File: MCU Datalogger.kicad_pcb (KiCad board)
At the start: 2 copper layers, 52.1 x 34.3 mm, 29 parts, among them J1 Conn_01x09_Pin, J2 Conn_01x04_Pin, J3 Conn_01x04_Pin, J4 Conn_02x03_Odd_Even, U1 24LC1025, U2 DS1337S_, U3 24LC1025, U4 ATMEGA328P-AU, Y1 32.768 KHz, Y2 16MHz

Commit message: Changes in Files.
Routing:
- net /SCK: track 0.00 -> 29.2 mm
- net /SDA: track 0.00 -> 17.6 mm
- net Net-(BT1-+): track 0.00 -> 13.3 mm
- net Net-(U2-SQW/~INT): track 0.00 -> 7.32 mm
- net Net-(U2-X2): track 0.00 -> 6.99 mm
- net Net-(U2-X1): track 0.00 -> 5.36 mm
- net Net-(U2-~{INTA}): track 0.00 -> 4.76 mm

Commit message: Completed wirings.
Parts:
- moved J1 1.27 mm to (94.6, 84.5)
- moved J3 1.27 mm to (120.0, 84.5)
- turned Y2 to 180 degrees
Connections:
- C5 pad 1: Net-(BT1-+) -> /Vcc
- D2 pad 2: Net-(BT1-+) -> /Vcc
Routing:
- net /SCK: track 29.2 -> 105.0 mm, vias 0 -> 7
- net /SDA: track 17.6 -> 69.6 mm, vias 0 -> 3
- net /TX: track 0.00 -> 36.8 mm
- net /RX: track 0.00 -> 33.8 mm
- net /D2: track 0.00 -> 32.7 mm
- net /D3: track 0.00 -> 28.0 mm
- net Net-(U4-PB6): track 0.00 -> 26.9 mm, vias 0 -> 3
- net /MOSI: track 0.00 -> 24.8 mm, vias 0 -> 2
- net /D4: track 0.00 -> 24.3 mm
- net /RESET: track 0.00 -> 24.3 mm, vias 0 -> 2
- net Net-(U4-PB7): track 0.00 -> 23.1 mm, vias 0 -> 3
- net /MISO: track 0.00 -> 20.9 mm, vias 0 -> 2
- net Net-(U4-AREF): track 0.00 -> 20.3 mm, vias 0 -> 2
- net /D8: track 0.00 -> 18.8 mm
- net /D7: track 0.00 -> 18.8 mm
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
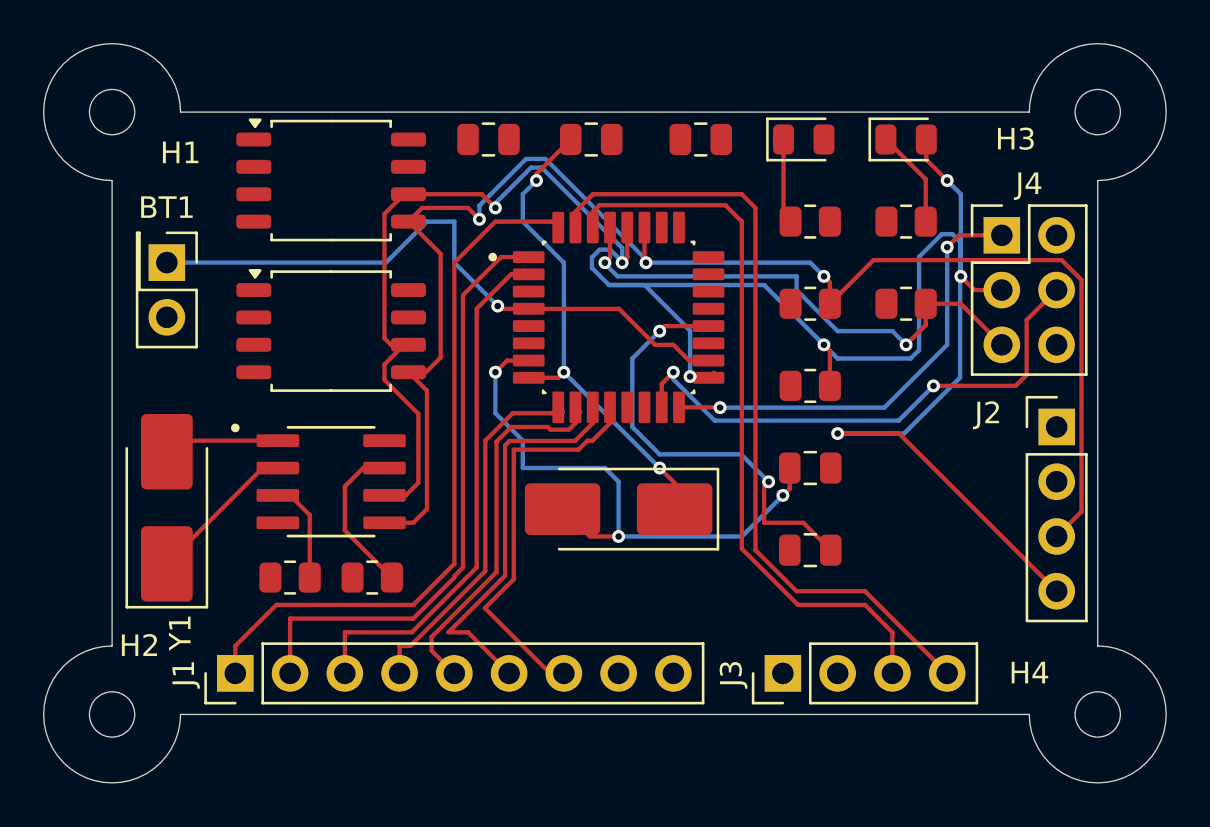
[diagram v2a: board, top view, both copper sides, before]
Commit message: Completed copper zones.
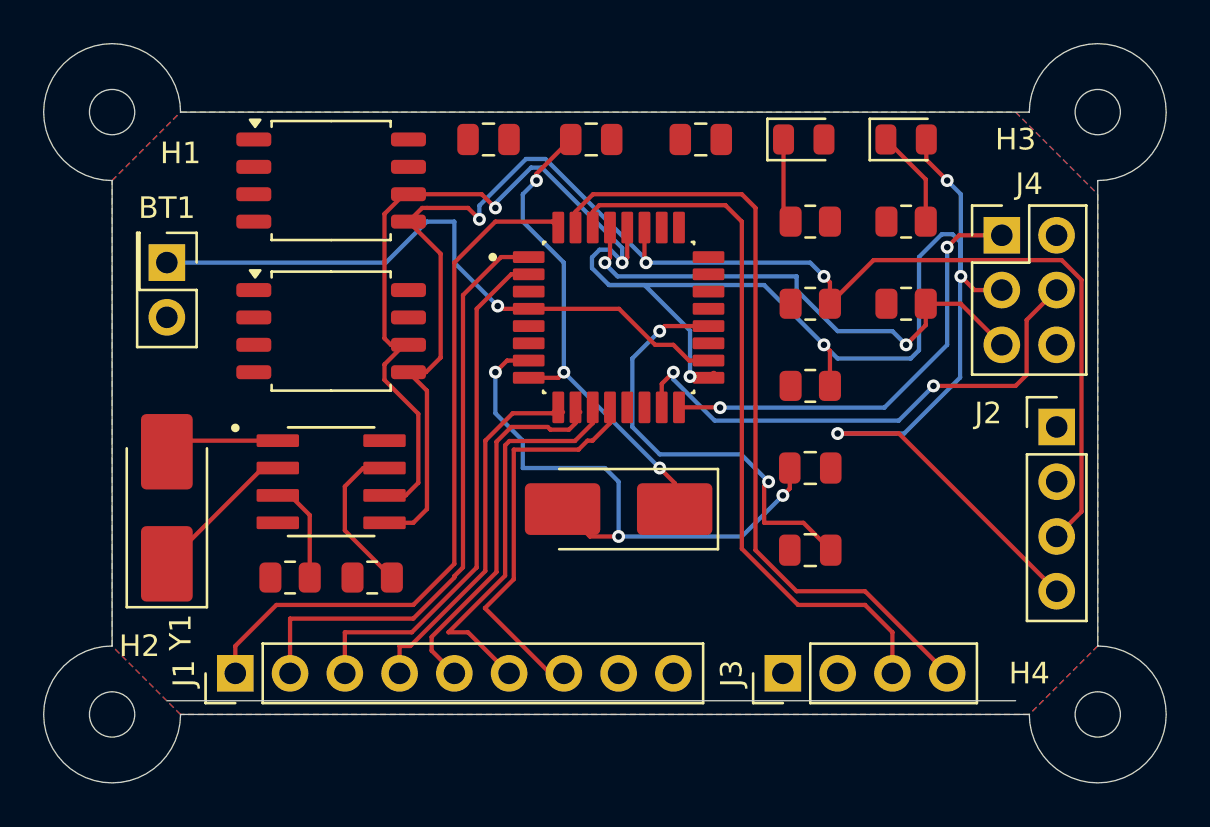
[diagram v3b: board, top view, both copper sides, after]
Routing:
- added copper zone on F.Cu, net /Vcc
- added copper zone on B.Cu, net GND
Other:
- outline, holes or cut-outs redrawn
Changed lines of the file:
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@@
+		(layer "Edge.Cuts")
+	)
+	(gr_line
+		(start 130.81 85.725)
+		(end 91.44 85.725)
+		(stroke
+			(width 0.05)
+			(type default)
+		)
 		(layer "Edge.Cuts")
 	)
@@
 		(net 26)
 	)
+	(zone
+		(net 3)
+		(net_name "/Vcc")
+		(layer "F.Cu")
+		(hatch edge 0.5)
+		(connect_pads
+			(clearance 0.5)
+		)
+		(min_thickness 0.25)
+		(filled_areas_thickness no)
+		(fill
+			(mode hatch)
+			(thermal_gap 0.5)
+			(thermal_bridge_width 0.5)
+			(hatch_thickness 1)
+			(hatch_gap 1.5)
+			(hatch_orientation 0)
+			(hatch_border_algorithm hatch_thickness)
+			(hatch_min_hole_area 0.3)
+		)
+		(polygon
+			(pts
+				(xy 88.9 61.595) (xy 92.075 58.42) (xy 130.81 58.42) (xy 134.62 62.23) (xy 134.62 83.185) (xy 131.445 86.36)
+				(xy 92.075 86.36) (xy 88.9 83.185)
+			)
+		)
+	)
+	(zone
+		(net 1)
+		(net_name "GND")
+		(layer "B.Cu")
+		(hatch edge 0.5)
+		(connect_pads
+			(clearance 0.5)
+		)
+		(min_thickness 0.25)
+		(filled_areas_thickness no)
+		(fill
+			(mode hatch)
+			(thermal_gap 0.5)
+			(thermal_bridge_width 0.5)
+			(hatch_thickness 1)
+			(hatch_gap 1.5)
+			(hatch_orientation 0)
+			(hatch_border_algorithm hatch_thickness)
+			(hatch_min_hole_area 0.3)
+		)
+		(polygon
+			(pts
+				(xy 88.9 61.595) (xy 92.075 58.42) (xy 130.81 58.42) (xy 134.62 62.23) (xy 134.62 83.185) (xy 131.445 86.36)
+				(xy 92.075 86.36) (xy 88.9 83.185)
+			)
+		)
+	)
 	(embedded_fonts no)

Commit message: Refined routing completed.
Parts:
- turned R5 to 180 degrees
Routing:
- net /Vcc: track 0.19 -> 138.8 mm, vias 0 -> 6
- net GND: track 0.00 -> 91.0 mm, vias 0 -> 11
- net /SCK: track 105.0 -> 116.9 mm, vias 7 -> 9
- net Net-(D2-K): track 3.95 -> 5.19 mm, vias 0 -> 2
- net Net-(D1-K): track 4.58 -> 3.82 mm
- net Net-(U2-X2): track 6.99 -> 7.36 mm, vias 0 -> 2
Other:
- outline, holes or cut-outs redrawn

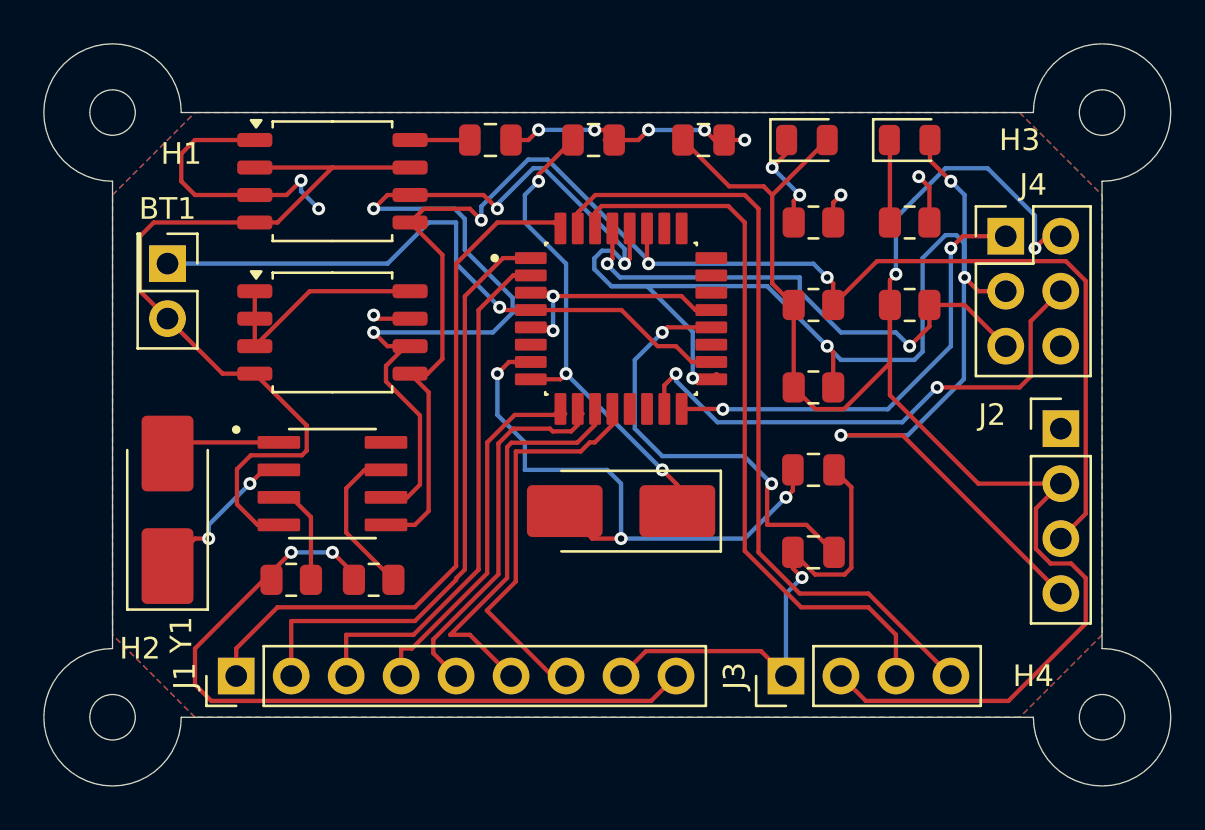
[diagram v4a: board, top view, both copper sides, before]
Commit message: Completed text references and value.
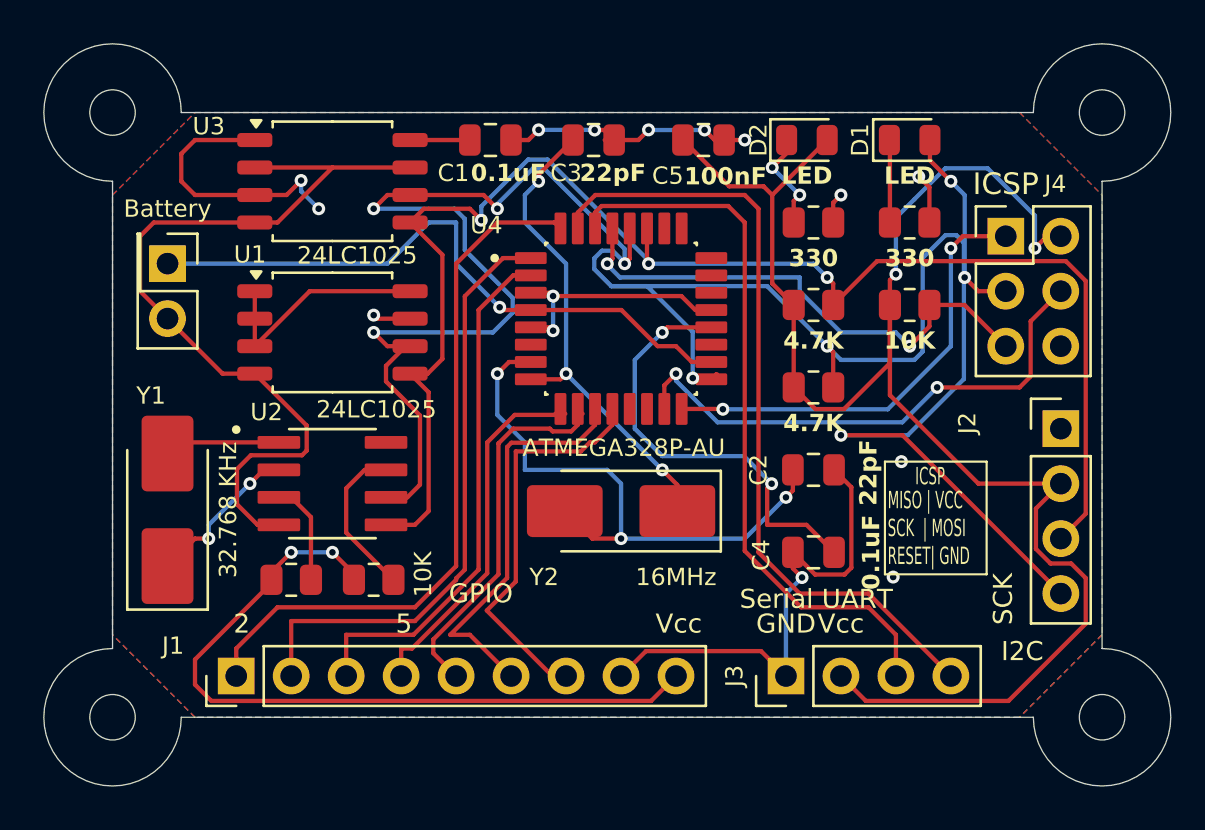
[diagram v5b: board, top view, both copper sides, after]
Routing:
- net (no net): vias 0 -> 2
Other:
- board text added: "ICSP"
- board text added: "MISO | VCC SCK | MOSI RESET| GND"

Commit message: Completed 2 layer.
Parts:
- added REF**: Symbol_GNU-Logo_SilkscreenTop, Symbol:Symbol_GNU-Logo_SilkscreenTop, B.Cu at (102.5, 74.0)
- added REF**: KiCad-Logo2_5mm_SilkScreen, Symbol:KiCad-Logo2_5mm_SilkScreen, B.Cu at (103.7, 64.1)
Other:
- board text added: "-2Mbit EEPROM -RTC -I2C, SPI, GPIO'S"
- board text added: "DATALOGGER WITH THE ATMEGA328P"

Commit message: Completed 2-layer PCB.
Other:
- board text added: "0.0000 mm / 0.0000 mm"
- board text added: "0.3000 mm"
- board text added: "1.6000 mm"
- board text added: "2"
- board text added: "52.0650 mm x 34.2850 mm"
- board text added: "BOARD CHARACTERISTICS"
- board text added: "Board Thickness:"
- board text added: "Board overall dimensions:"
- board text added: "Castellated pads:"
- board text added: "Copper Finish:"
- board text added: "Copper Layer Count:"
- board text added: "Edge card connectors:"
- board text added: "Impedance Control:"
- board text added: "Min hole diameter:"
- board text added: "Min track/spacing:"
- board text added: "No"
- board text added: "None"
- board text added: "Plated Board Edge:"

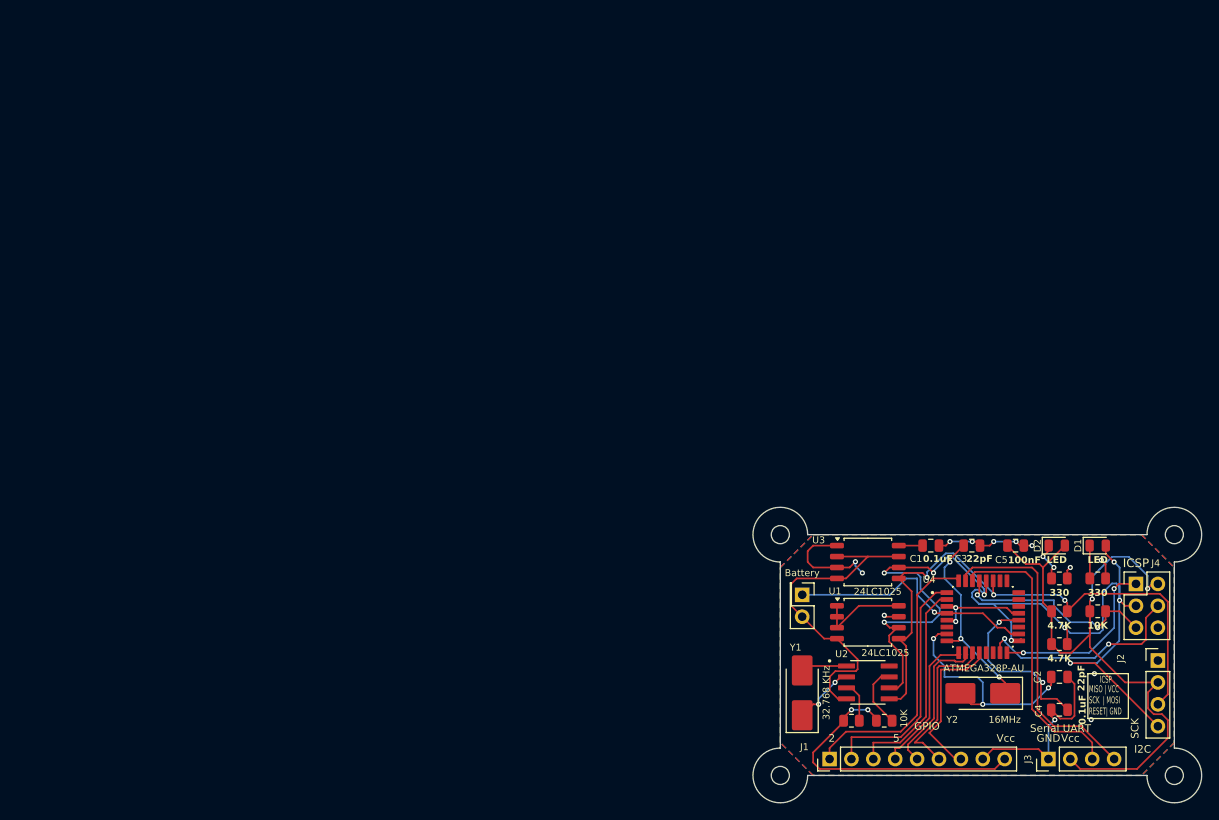
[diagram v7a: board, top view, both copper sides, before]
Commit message: Fixed two defects in the schematic.
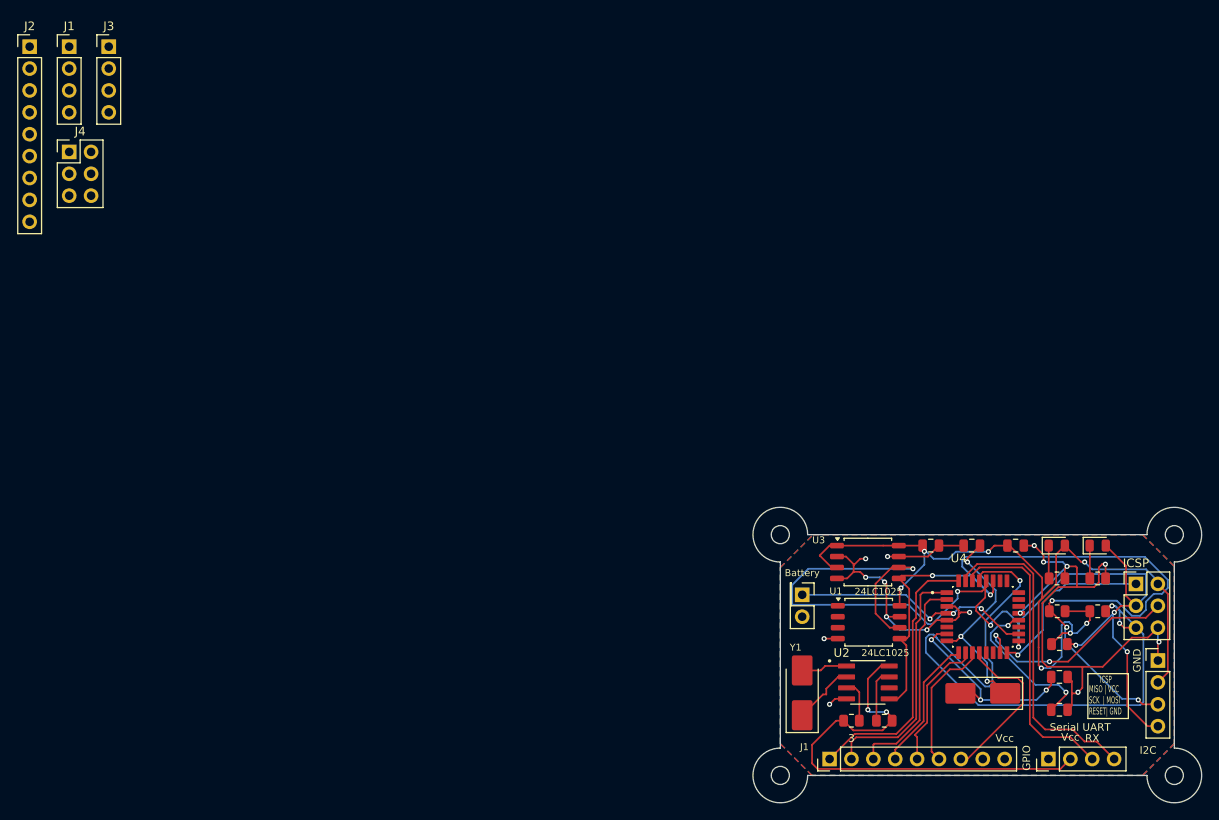
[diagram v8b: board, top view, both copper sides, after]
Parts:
- added J1: Conn_01x04_Pin, Connector_PinHeader_2.54mm:PinHeader_1x04_P2.54mm_Vertical, F.Cu at (6.38, 1.79)
- added J2: Conn_01x09_Pin, Connector_PinHeader_2.54mm:PinHeader_1x09_P2.54mm_Vertical, F.Cu at (1.79, 1.79)
- added J3: Conn_01x04_Pin, Connector_PinHeader_2.54mm:PinHeader_1x04_P2.54mm_Vertical, F.Cu at (11.0, 1.79)
- added J4: Conn_02x03_Odd_Even, Connector_PinHeader_2.54mm:PinHeader_2x03_P2.54mm_Vertical, F.Cu at (6.38, 14.0)
- U2: footprint FOOTPRINTS:DS13375+ -> DS13375:DS13375
- U4: footprint FOOTPRINTS:ATMEGA -> ATMEGA:ATMEGA
- moved REF** 2.75 mm to (102.5, 71.2)
- moved R7 0.28 mm to (121.0, 63.5)
- moved R4 0.25 mm to (121.0, 67.3), turned to 180 degrees
- moved U1 0.10 mm to (99.2, 68.6)
- turned C3 to 180 degrees
- turned C4 to 180 degrees
- turned R2 to 180 degrees
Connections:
- net Net-(U4-AREF) renamed /Abc123
- C5 pad 1: /Vcc -> Net-(BT1-+)
- D2 pad 2: /Vcc -> Net-(BT1-+)
- U2 pad 6: /SCK -> /SCL
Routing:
- net /RESET: track 24.3 -> 78.6 mm, vias 2 -> 3
- net /SDA: track 69.6 -> 97.8 mm, vias 3 -> 5
- net GND: track 91.0 -> 108.5 mm, vias 11 -> 16
- net /Vcc: track 138.6 -> 155.7 mm, vias 6 -> 9
- net /SCK: track 116.9 -> 128.7 mm, vias 9 -> 7
- net /D7: track 18.8 -> 15.5 mm
- net Net-(U4-PB6): track 26.9 -> 23.9 mm
- net Net-(U4-PB7): track 23.1 -> 25.2 mm
- net /D6: track 17.6 -> 15.7 mm
- net /Abc123: track 20.3 -> 18.7 mm
- net Net-(BT1-+): track 29.7 -> 28.2 mm, vias 1 -> 3
- net Net-(D2-K): track 5.19 -> 3.83 mm, vias 2 -> 0
- net /D5: track 17.1 -> 15.7 mm
- net Net-(U2-SQW/~INT): track 7.32 -> 6.27 mm
- net /D2: track 32.7 -> 31.8 mm
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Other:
- copper layers 2 -> 4
- board text added: "JESIER CRESENCIO BSECE 1C"
- board text removed: "0.0000 mm / 0.0000 mm"
- board text removed: "0.3000 mm"
- board text removed: "1.6000 mm"
- board text removed: "2"
- board text removed: "52.0650 mm x 34.2850 mm"
- board text removed: "BOARD CHARACTERISTICS"
- board text removed: "Board Thickness:"
- board text removed: "Board overall dimensions:"
- board text removed: "Castellated pads:"
- board text removed: "Copper Finish:"
- board text removed: "Copper Layer Count:"
- board text removed: "Edge card connectors:"
- board text removed: "Impedance Control:"
- board text removed: "Min hole diameter:"
- board text removed: "Min track/spacing:"
- board text removed: "No"
- board text removed: "None"
- board text removed: "Plated Board Edge:"
